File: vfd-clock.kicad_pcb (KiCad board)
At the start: 2 copper layers, 139.7 x 49.5 mm, 31 parts, among them CON1 BARREL_JACK_2, CON2 BARREL_JACK_2, P1 ST_LINK, SW1 SET, SW2 UP, SW3 DOWN, U1 Maple_Mini_(BTE14-07), U2 CD4056, U3 CD4056, U4 CD4056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

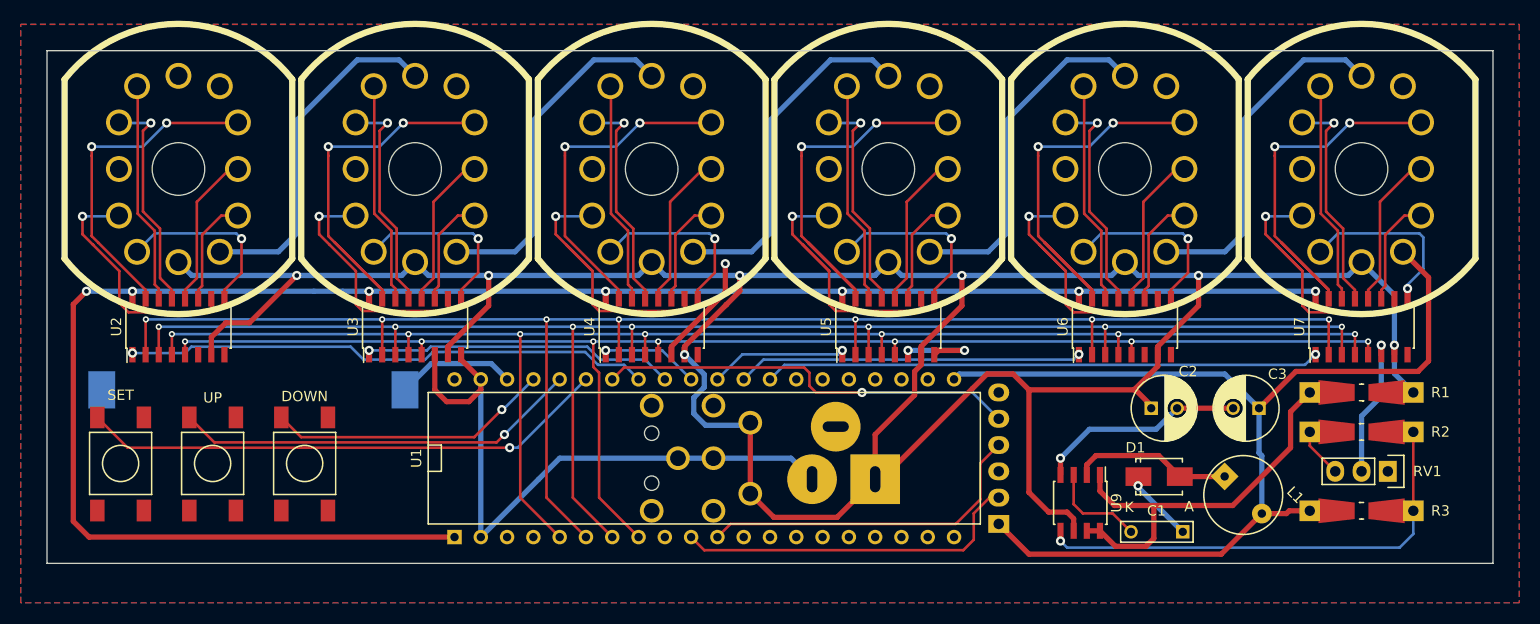
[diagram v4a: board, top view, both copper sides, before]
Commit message: lots of rerouting, buttons, part switches
surface mount!
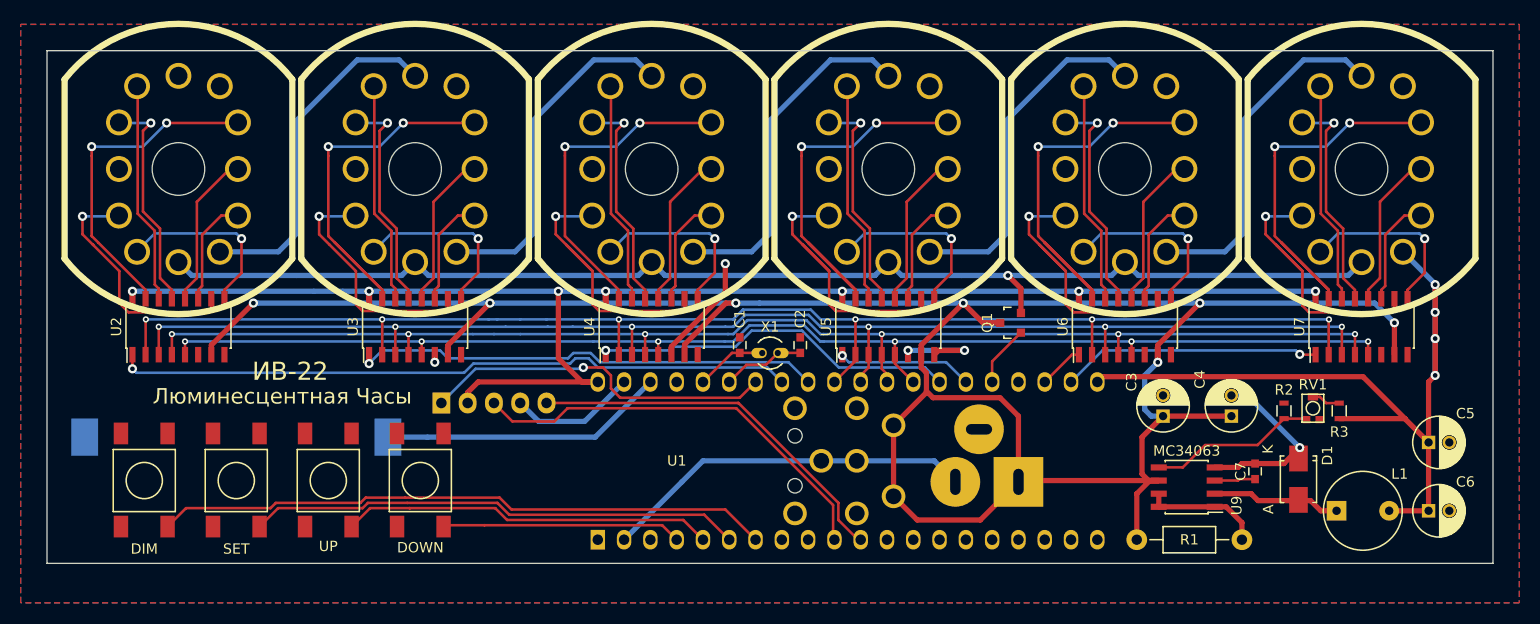
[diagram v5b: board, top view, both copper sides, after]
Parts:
- added C4: 47u, Capacitors_ThroughHole:C_Radial_D5_L11_P2, F.Cu at (129.7, 50.5)
- added C5: 47u, Capacitors_ThroughHole:C_Radial_D5_L11_P2, F.Cu at (148.7, 53.1)
- added C6: 47u, Capacitors_ThroughHole:C_Radial_D5_L11_P2, F.Cu at (148.7, 59.7)
- added C7: 330p, Capacitors_SMD:C_0603, F.Cu at (132.0, 55.9)
- added Q1: 2N7002P, Housings_SOT-23_SOT-143_TSOT-6:SOT-23, F.Cu at (108.3, 41.5)
- added SW4: DIM, VFD:SMD_TACT_6mm, F.Cu at (24.6, 56.8)
- added X1: CRYSTAL, Crystals:Crystal_Round_Vertical_3mm_BigPad, F.Cu at (85.1, 44.5)
- C1: value 330p -> 18p; footprint Capacitors_ThroughHole:C_Rect_L7_W2_P5 -> Capacitors_SMD:C_0603
- C2: value 100u -> 18p; footprint Capacitors_ThroughHole:C_Radial_D6.3_L11.2_P2.5 -> Capacitors_SMD:C_0603
- C3: value 100u -> 47u; footprint Capacitors_ThroughHole:C_Radial_D6.3_L11.2_P2.5 -> Capacitors_ThroughHole:C_Radial_D5_L11_P2
- P1: footprint Pin_Headers:Pin_Header_Angled_1x06 -> Pin_Headers:Pin_Header_Angled_1x05
- R1: footprint Resistors_Universal:Resistor_SMD+THTuniversal_0805to1206_RM10_HandSoldering -> Resistors_ThroughHole:Resistor_Horizontal_RM10mm
- R2: value 12k -> 12.4k; footprint Resistors_Universal:Resistor_SMD+THTuniversal_0805to1206_RM10_HandSoldering -> Resistors_SMD:R_0603
- R3: value 59.5k -> 54k9; footprint Resistors_Universal:Resistor_SMD+THTuniversal_0805to1206_RM10_HandSoldering -> Resistors_SMD:R_0603
- RV1: value 1k -> 4k7; footprint Pin_Headers:Pin_Header_Straight_1x03 -> VFD:PVA2_POT
- U1: footprint Sockets_DIP:DIP-40__600 -> VFD:Maple_Mini_(BTE14-07)
- moved P1 55.1 mm to (53.3, 49.3), turned to 270 degrees
- moved C1 46.4 mm to (82.2, 43.7), turned to 90 degrees
- moved C2 34.5 mm to (88.0, 43.7), turned to 90 degrees
- moved R1 21.9 mm to (125.6, 62.5), turned to 0 degrees
- moved CON1 13.8 mm to (103.0, 56.9)
- moved CON2 13.8 mm to (90.8, 54.9)
- moved U1 13.8 mm to (92.6, 54.9)
- moved D1 13.5 mm to (136.1, 56.6), turned to 270 degrees
- moved L1 11.7 mm to (142.4, 59.7), turned to 0 degrees
- moved SW3 11.3 mm to (51.3, 56.8), turned to 270 degrees
- moved SW1 11.3 mm to (33.5, 56.8), turned to 270 degrees
- moved SW2 11.3 mm to (42.4, 56.8), turned to 270 degrees
- moved U9 10.4 mm to (125.3, 57.4), turned to 180 degrees
- moved R3 9.89 mm to (140.1, 50.0), turned to 270 degrees
- moved RV1 9.46 mm to (137.5, 49.8), turned to 0 degrees
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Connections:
- C1 pad 1: /GND -> Net-(C1-Pad1)
- C1 pad 2: Net-(C1-Pad2) -> /GND
- C2 pad 1: /19v5 -> Net-(C2-Pad1)
- C3 pad 1: /7v2 -> /19v5
- P1 pad 1: /7v2 -> /RST
- P1 pad 2: /SWCLK -> /3v3
- P1 pad 3: /GND -> /SWCLK
- P1 pad 4: /SWDIO -> /GND
- P1 pad 5: /RST -> /SWDIO
- R2 pad 2: Net-(R2-Pad2) -> /GND
- R3 pad 1: /7v2 -> Net-(R3-Pad1)
- R3 pad 2: Net-(R2-Pad2) -> /7v2
- RV1 pad 1: (no net) -> Net-(R2-Pad1)
- RV1 pad 2: /GND -> Net-(R3-Pad1)
- RV1 pad 3: Net-(R2-Pad1) -> (no net)
- U1 pad 1: /3v3 -> (no net)
- U1 pad 22: (no net) -> /STROBE6
- U1 pad 23: (no net) -> /STROBE5
- U1 pad 25: (no net) -> /GRID_PWM
- U1 pad 26: (no net) -> /STROBE4
- U1 pad 27: (no net) -> /STROBE3
- U1 pad 28: /STROBE6 -> /DA
- U1 pad 29: /STROBE5 -> /DD
- U1 pad 30: /STROBE4 -> /DB
- U1 pad 31: /STROBE3 -> /DC
- U1 pad 35: /BTN_SET -> Net-(C2-Pad1)
- U1 pad 36: /BTN_UP -> Net-(C1-Pad1)
- U1 pad 37: /BTN_DN -> (no net)
- U1 pad 4: (no net) -> /BTN_DN
- U1 pad 40: (no net) -> /3v3
- U1 pad 5: /DD -> /BTN_UP
- U1 pad 6: /DC -> /BTN_SET
- U1 pad 7: /DB -> /BTN_DIM
- U1 pad 8: /DA -> (no net)
- U9 pad 3: Net-(C1-Pad2) -> Net-(C7-Pad2)
- U9 pad 5: Net-(R2-Pad2) -> Net-(R2-Pad1)
- V1 pad 6: /19v5 -> /GRID
- V2 pad 6: /19v5 -> /GRID
- V3 pad 6: /19v5 -> /GRID
- V4 pad 6: /19v5 -> /GRID
- V5 pad 6: /19v5 -> /GRID
- V6 pad 6: /19v5 -> /GRID
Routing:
- net /GRID: track 0.00 -> 123.8 mm, vias 0 -> 1
- net /BTN_DIM: track 0.00 -> 59.6 mm
- net Net-(R2-Pad2): track 50.9 -> 0.00 mm, vias 1 -> 0
- net /19v5: track 289.5 -> 243.2 mm
- net /3v3: track 183.3 -> 143.9 mm
- net /GND: track 125.5 -> 87.2 mm, vias 6 -> 5
- net /REG_HI: track 42.1 -> 11.6 mm
- net /STROBE5: track 33.4 -> 4.39 mm, vias 1 -> 0
- net /STROBE6: track 53.7 -> 25.1 mm
- net /7v2: track 106.8 -> 80.6 mm, vias 0 -> 4
- net /STROBE3: track 9.83 -> 35.5 mm
- net /DC: track 157.4 -> 139.0 mm, vias 7 -> 6
- net /DB: track 152.4 -> 134.4 mm, vias 7 -> 6
- net /DD: track 147.4 -> 130.2 mm, vias 7 -> 6
- net /Vbat: track 11.5 -> 27.6 mm
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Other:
- board text added: "RST 3v3 CLK GND DIO"
- board text added: "ИB-22"
- board text added: "Люминесцентная Часы"
